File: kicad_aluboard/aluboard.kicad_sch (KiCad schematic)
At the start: 78 parts, among them J1 backplane 2, J2 backplane 1, J3 disp_adlow, J4 disp_adhigh, U1 am2901, U10 am2901, U11 am2901, U2 74LS151, U3 74LS00, U4 74LS00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

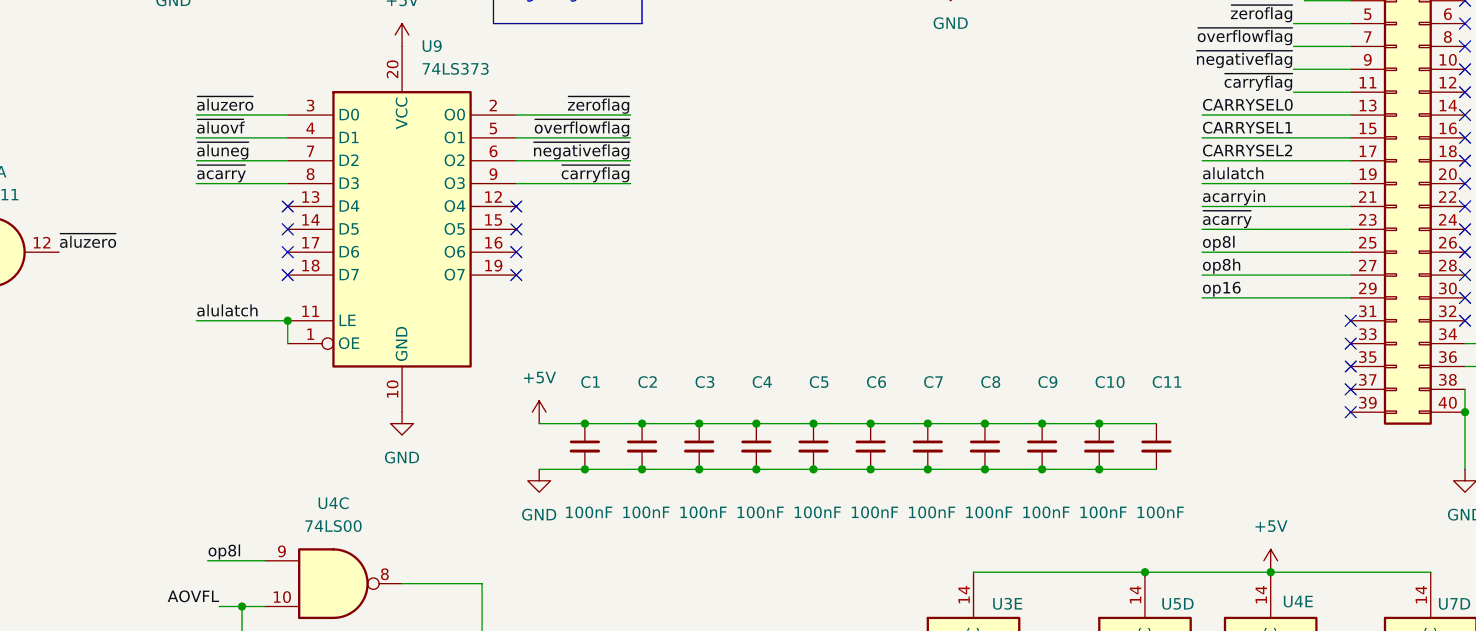
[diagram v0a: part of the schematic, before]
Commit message: Redoing control board because of pipeline blunder. This also is the last version with the distinct program counter.
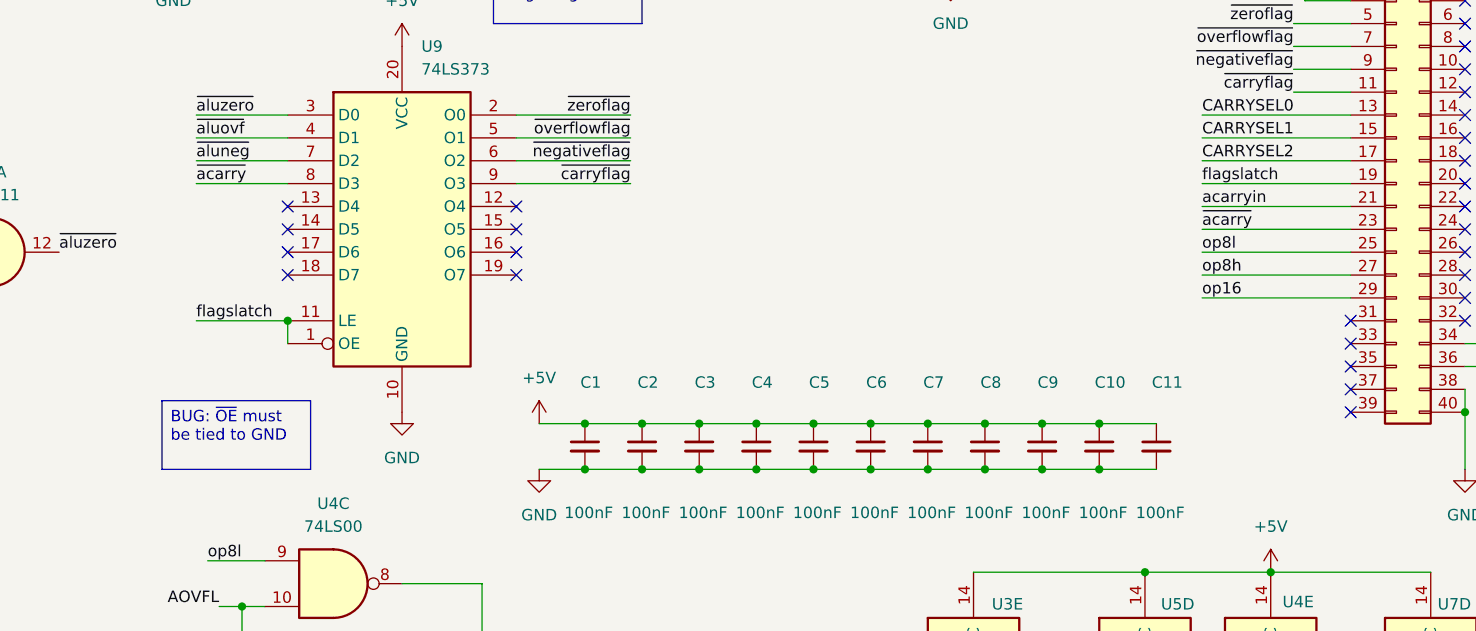
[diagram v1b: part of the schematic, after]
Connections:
- net alulatch renamed flagslatch
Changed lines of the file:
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@@
 		)
 	)
+	(text_box "BUG: ~{OE} must be tied to GND"
+		(exclude_from_sim no)
+		(at 149.86 217.17 0)
+		(size 16.51 7.62)
+		(margins 0.9525 0.9525 0.9525 0.9525)
+		(stroke
+			(width 0)
+			(type solid)
+		)
+		(fill
+			(type color)
+			(color 255 0 0 1)
+		)
+		(effects
+			(font
+				(size 1.27 1.27)
+			)
+			(justify left top)
+		)
+	)
 	(text_box "ALU Dest"
 		(exclude_from_sim no)
@@
 		)
 	)
-	(label "alulatch"
+	(label "flagslatch"
 		(at 265.43 193.04 0)
 		(effects
@@
 		)
 	)
-	(label "alulatch"
+	(label "flagslatch"
 		(at 153.67 208.28 0)
 		(effects
